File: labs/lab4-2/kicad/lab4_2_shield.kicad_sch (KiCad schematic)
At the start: 31 parts, among them J1 Digital_0-7, J2 Digital_8-13, J3 Power, J4 Analog_In, Q1 2N3904, Q2 2N3904, SW1 SW_Push, SW2 SW_Push, SW3 SW_Push, SW4 SW_Push

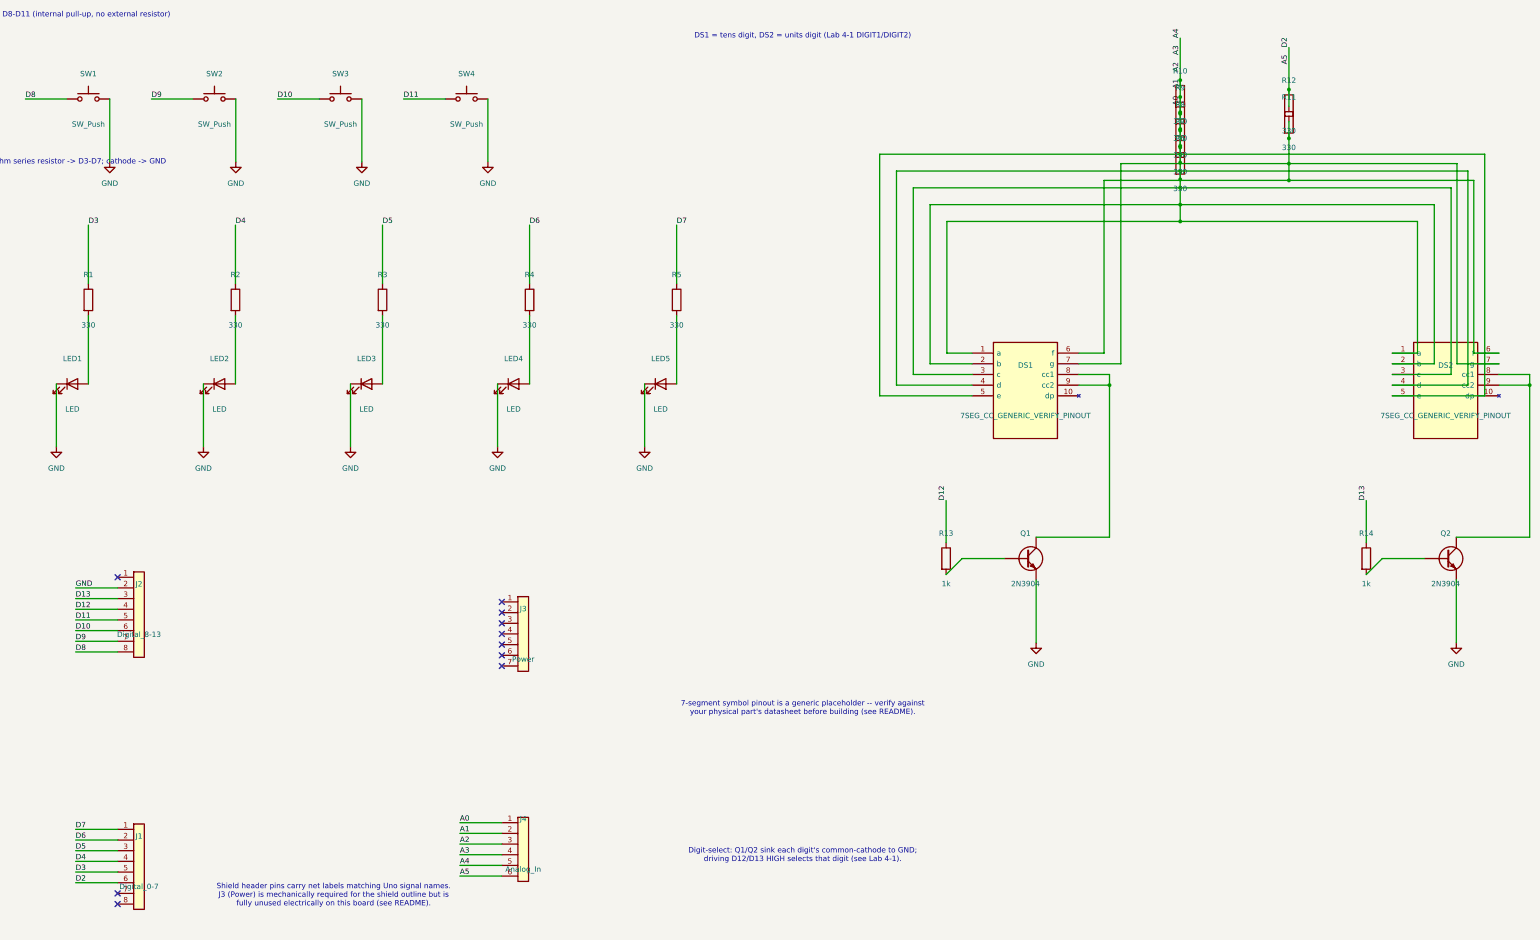
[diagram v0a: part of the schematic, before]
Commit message: feat: add LTS-6980HR 7-segment display and update KiCad project configurations
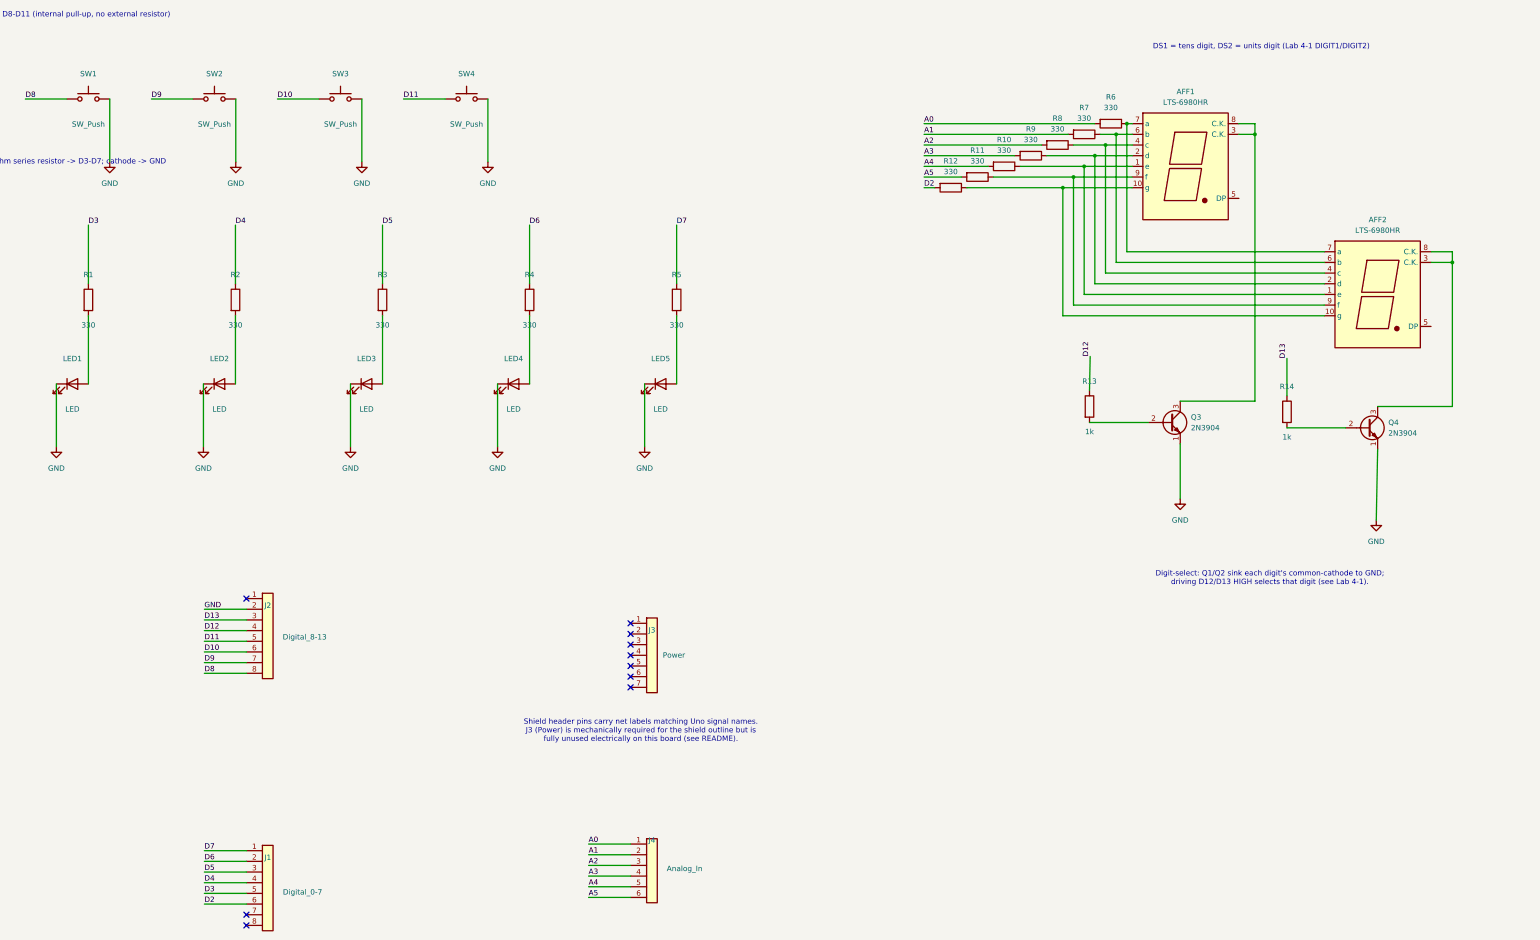
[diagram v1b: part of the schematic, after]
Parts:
- removed DS1, DS2: 7SEG_CC_GENERIC_VERIFY_PINOUT, lab4_2_shield:DISPLAY_7SEG_CC_GENERIC, symbol lab4_2_shield:DISPLAY_7SEG_CC
- removed Q1, Q2: 2N3904, Package_TO_SOT_THT:TO-92_Inline, symbol Device:Q_NPN
- added AFF1, AFF2: LTS-6980HR, Display_7Segment:7SegmentLED_LTS6760_LTS6780, symbol Display_Character:LTS-6980HR
- added Q3, Q4: 2N3904, Package_TO_SOT_THT:TO-92_Inline, symbol Transistor_BJT:2N3904
- J1, J2: footprint lab4_2_shield:Header_Shield_Female_1x08_P2.54mm -> Connector_PinHeader_2.54mm:PinHeader_1x08_P2.54mm_Vertical
- J3: footprint lab4_2_shield:Header_Shield_Female_1x07_P2.54mm -> Connector_PinHeader_2.54mm:PinHeader_1x07_P2.54mm_Vertical
- J4: footprint lab4_2_shield:Header_Shield_Female_1x06_P2.54mm -> Connector_PinHeader_2.54mm:PinHeader_1x06_P2.54mm_Vertical
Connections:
- net A0: no longer J4.2 (Pin_2), J4.3 (Pin_3), J4.4 (Pin_4), J4.5 (Pin_5), R10.1, R10.2, R6.1, R7.1, R7.2, R8.1, R8.2, R9.1, R9.2
- net A5: now also R11.2; no longer J1.6 (Pin_6), R11.1, R12.1
- net GND: now also Q3.1 (E), Q4.1 (E)
- net D2: now reaches R12.2
- net D2: now also J1.6 (Pin_6); no longer R11.2
- net at R13.2: now also Q3.2 (B)
- net at R14.2: now also Q4.2 (B)
- new net: AFF1.7 (a), AFF2.7 (a), R6.1
- new net: AFF1.6 (b), AFF2.6 (b), R7.1
- new net: AFF1.3 (C.K.), AFF1.8 (C.K.), Q3.3 (C)
- new net: AFF1.1 (e), AFF2.1 (e), R10.1
- new net: AFF1.10 (g), AFF2.10 (g), R12.1
- new net: AFF1.2 (d), AFF2.2 (d), R9.1
- new net: AFF1.4 (c), AFF2.4 (c), R8.1
- new net: AFF1.9 (f), AFF2.9 (f), R11.1
- new net: AFF2.3 (C.K.), AFF2.8 (C.K.), Q4.3 (C)
- new net A1: J4.2 (Pin_2), R7.2
- new net A2: J4.3 (Pin_3), R8.2
- new net A3: J4.4 (Pin_4), R9.2
- new net A4: J4.5 (Pin_5), R10.2
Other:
- note removed: "7-segment symbol pinout is a generic placeholder -- verify against your physical part's datasheet before building (see README)."
- moved on the sheet: J1, J2, J3, J4, R13, R14

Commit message: feat: initialize KiCad project files and PCB layout for lab 4.2 shield
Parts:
- renumbered J2 to J1, J1 to J2, Q3 to Q1, Q4 to Q2, R8 to R10, R7 to R11, R13 to R12, R6 to R13, R12 to R6, R11 to R7, R10 to R8
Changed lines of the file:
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@@
 		(in_pos_files yes)
 		(dnp no)
-		(property "Reference" "#PWR009"
+		(property "Reference" "#PWR09"
 			(at 187.49 156.95 0)
 			(hide yes)
@@
 			(project "lab4_2_shield"
 				(path "/d2732c36-58ec-418a-9ad1-28d53cb8d85c"
-					(reference "#PWR009")
+					(reference "#PWR09")
 					(unit 1)
 				)
@@
 		(dnp no)
 		(fields_autoplaced yes)
-		(property "Reference" "R6"
+		(property "Reference" "R13"
 			(at 298.45 67.31 90)
 			(show_name no)
@@
 			(project "lab4_2_shield"
 				(path "/d2732c36-58ec-418a-9ad1-28d53cb8d85c"
-					(reference "R6")
+					(reference "R13")
 					(unit 1)
 				)
@@
 		(dnp no)
 		(fields_autoplaced yes)
-		(property "Reference" "R7"
+		(property "Reference" "R11"
 			(at 292.1 69.85 90)
 			(show_name no)
@@
 			(project "lab4_2_shield"
 				(path "/d2732c36-58ec-418a-9ad1-28d53cb8d85c"
-					(reference "R7")
+					(reference "R11")
 					(unit 1)
 				)
@@
 		(dnp no)
 		(fields_autoplaced yes)
-		(property "Reference" "Q3"
+		(property "Reference" "Q1"
 			(at 317.5 143.5099 0)
 			(show_name no)
@@
 			(project "lab4_2_shield"
 				(path "/d2732c36-58ec-418a-9ad1-28d53cb8d85c"
-					(reference "Q3")
+					(reference "Q1")
 					(unit 1)
 				)
@@
 		(dnp no)
 		(fields_autoplaced yes)
-		(property "Reference" "R11"
+		(property "Reference" "R7"
 			(at 266.7 80.01 90)
 			(show_name no)
@@
 			(project "lab4_2_shield"
 				(path "/d2732c36-58ec-418a-9ad1-28d53cb8d85c"
-					(reference "R11")
+					(reference "R7")
 					(unit 1)
 				)
@@
 		(in_pos_files yes)
 		(dnp no)
-		(property "Reference" "J1"
+		(property "Reference" "J2"
 			(at 97.79 248.31 0)
 			(show_name no)
@@
 			(project "lab4_2_shield"
 				(path "/d2732c36-58ec-418a-9ad1-28d53cb8d85c"
-					(reference "J1")
+					(reference "J2")
 					(unit 1)
 				)
@@
 		(in_pos_files yes)
 		(dnp no)
-		(property "Reference" "R13"
+		(property "Reference" "R12"
 			(at 293.37 134.97 0)
 			(show_name no)
@@
 			(project "lab4_2_shield"
 				(path "/d2732c36-58ec-418a-9ad1-28d53cb8d85c"
-					(reference "R13")
+					(reference "R12")
 					(unit 1)
 				)
@@
 		(in_pos_files yes)
 		(dnp no)
-		(property "Reference" "#PWR001"
+		(property "Reference" "#PWR02"
 			(at 60.19 89.14 0)
 			(hide yes)
@@
 			(project "lab4_2_shield"
 				(path "/d2732c36-58ec-418a-9ad1-28d53cb8d85c"
-					(reference "#PWR001")
+					(reference "#PWR02")
 					(unit 1)
 				)
@@
 		(in_pos_files yes)
 		(dnp no)
-		(property "Reference" "#PWR002"
+		(property "Reference" "#PWR04"
 			(at 90.19 89.14 0)
 			(hide yes)
@@
 			(project "lab4_2_shield"
 				(path "/d2732c36-58ec-418a-9ad1-28d53cb8d85c"
-					(reference "#PWR002")
+					(reference "#PWR04")
 					(unit 1)
 				)
@@
 		(in_pos_files yes)
 		(dnp no)
-		(property "Reference" "#PWR005"
+		(property "Reference" "#PWR01"
 			(at 47.49 156.95 0)
 			(hide yes)
@@
 			(project "lab4_2_shield"
 				(path "/d2732c36-58ec-418a-9ad1-28d53cb8d85c"
-					(reference "#PWR005")
+					(reference "#PWR01")
 					(unit 1)
 				)
@@
 		(in_pos_files yes)
 		(dnp no)
-		(property "Reference" "#PWR008"
+		(property "Reference" "#PWR08"
 			(at 152.49 156.95 0)
 			(hide yes)
@@
 			(project "lab4_2_shield"
 				(path "/d2732c36-58ec-418a-9ad1-28d53cb8d85c"
-					(reference "#PWR008")
+					(reference "#PWR08")
 					(unit 1)
 				)
@@
 		(in_pos_files yes)
 		(dnp no)
-		(property "Reference" "#PWR003"
+		(property "Reference" "#PWR06"
 			(at 120.19 89.14 0)
 			(hide yes)
@@
 			(project "lab4_2_shield"
 				(path "/d2732c36-58ec-418a-9ad1-28d53cb8d85c"
-					(reference "#PWR003")
+					(reference "#PWR06")
 					(unit 1)
 				)
@@
 		(dnp no)
 		(fields_autoplaced yes)
-		(property "Reference" "R10"
+		(property "Reference" "R8"
 			(at 273.05 77.47 90)
 			(show_name no)
@@
 			(project "lab4_2_shield"
 				(path "/d2732c36-58ec-418a-9ad1-28d53cb8d85c"
-					(reference "R10")
+					(reference "R8")
 					(unit 1)
 				)
@@
 		(in_pos_files yes)
 		(dnp no)
-		(property "Reference" "#PWR006"
+		(property "Reference" "#PWR03"
 			(at 82.49 156.95 0)
 			(hide yes)
@@
 			(project "lab4_2_shield"
 				(path "/d2732c36-58ec-418a-9ad1-28d53cb8d85c"
-					(reference "#PWR006")
+					(reference "#PWR03")
 					(unit 1)
 				)
@@
 		(in_pos_files yes)
 		(dnp no)
-		(property "Reference" "#PWR007"
+		(property "Reference" "#PWR05"
 			(at 117.49 156.95 0)
 			(hide yes)
@@
 			(project "lab4_2_shield"
 				(path "/d2732c36-58ec-418a-9ad1-28d53cb8d85c"
-					(reference "#PWR007")
+					(reference "#PWR05")
 					(unit 1)
 				)
@@
 		(dnp no)
 		(fields_autoplaced yes)
-		(property "Reference" "R12"
+		(property "Reference" "R6"
 			(at 260.35 82.55 90)
 			(show_name no)
@@
 			(project "lab4_2_shield"
 				(path "/d2732c36-58ec-418a-9ad1-28d53cb8d85c"
-					(reference "R12")
+					(reference "R6")
 					(unit 1)
 				)
@@
 		(dnp no)
 		(fields_autoplaced yes)
-		(property "Reference" "R8"
+		(property "Reference" "R10"
 			(at 285.75 72.39 90)
 			(show_name no)
@@
 			(project "lab4_2_shield"
 				(path "/d2732c36-58ec-418a-9ad1-28d53cb8d85c"
-					(reference "R8")
+					(reference "R10")
 					(unit 1)
 				)
@@
 		(in_pos_files yes)
 		(dnp no)
-		(property "Reference" "#PWR004"
+		(property "Reference" "#PWR07"
 			(at 150.19 89.14 0)
 			(hide yes)
@@
 			(project "lab4_2_shield"
 				(path "/d2732c36-58ec-418a-9ad1-28d53cb8d85c"
-					(reference "#PWR004")
+					(reference "#PWR07")
 					(unit 1)
 				)
@@
 		(dnp no)
 		(fields_autoplaced yes)
-		(property "Reference" "Q4"
+		(property "Reference" "Q2"
 			(at 364.49 144.7799 0)
 			(show_name no)
@@
 			(project "lab4_2_shield"
 				(path "/d2732c36-58ec-418a-9ad1-28d53cb8d85c"
-					(reference "Q4")
+					(reference "Q2")
 					(unit 1)
 				)
@@
 		(in_pos_files yes)
 		(dnp no)
-		(property "Reference" "J2"
+		(property "Reference" "J1"
 			(at 97.79 188.31 0)
 			(show_name no)
@@
 			(project "lab4_2_shield"
 				(path "/d2732c36-58ec-418a-9ad1-28d53cb8d85c"
-					(reference "J2")
-					(unit 1)
-				)
+					(reference "J1")
+					(unit 1)
+				)

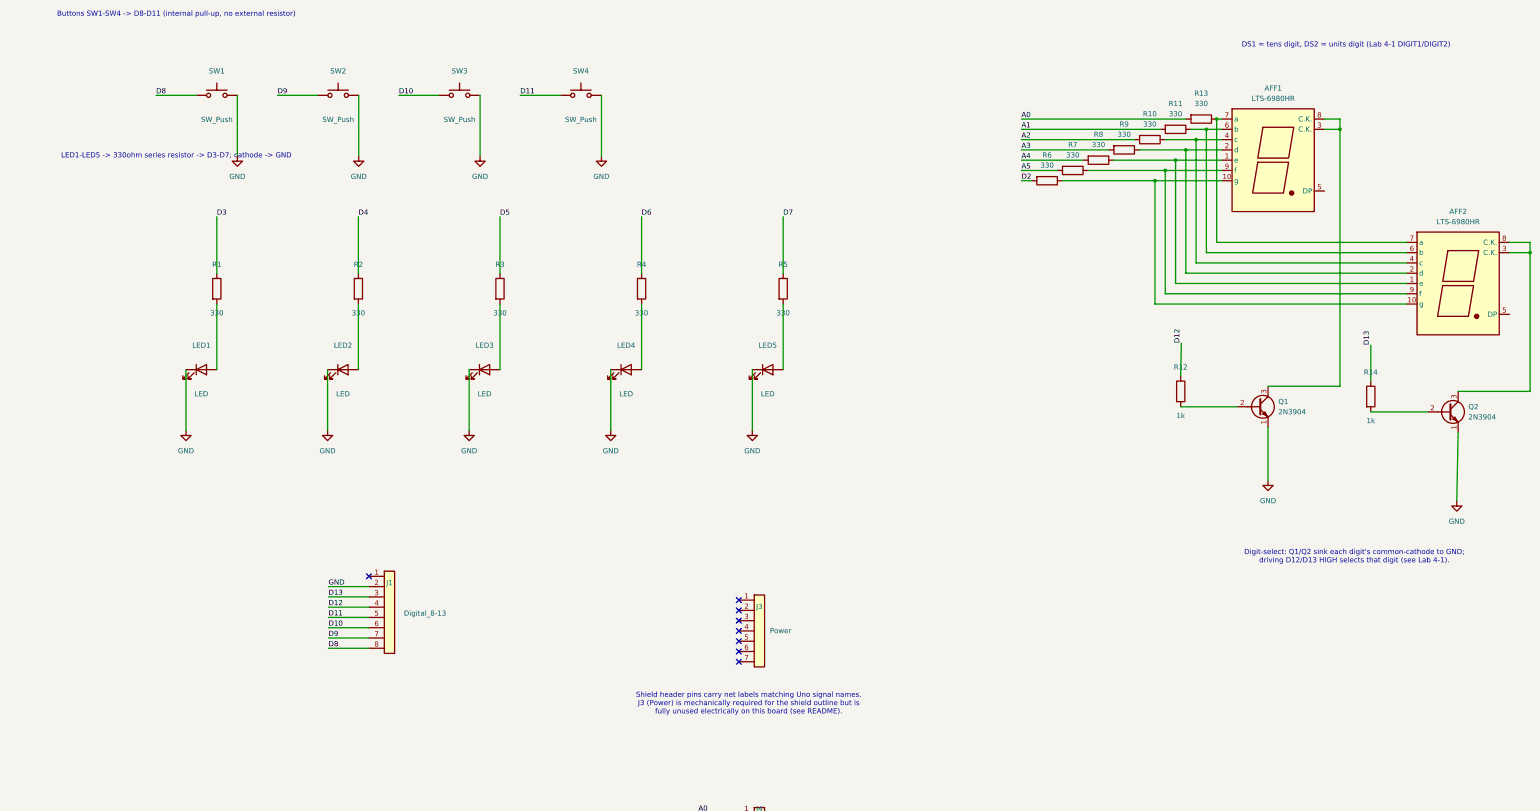
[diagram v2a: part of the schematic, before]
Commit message: refactor: update text label coordinates and component placements in KiCad project files
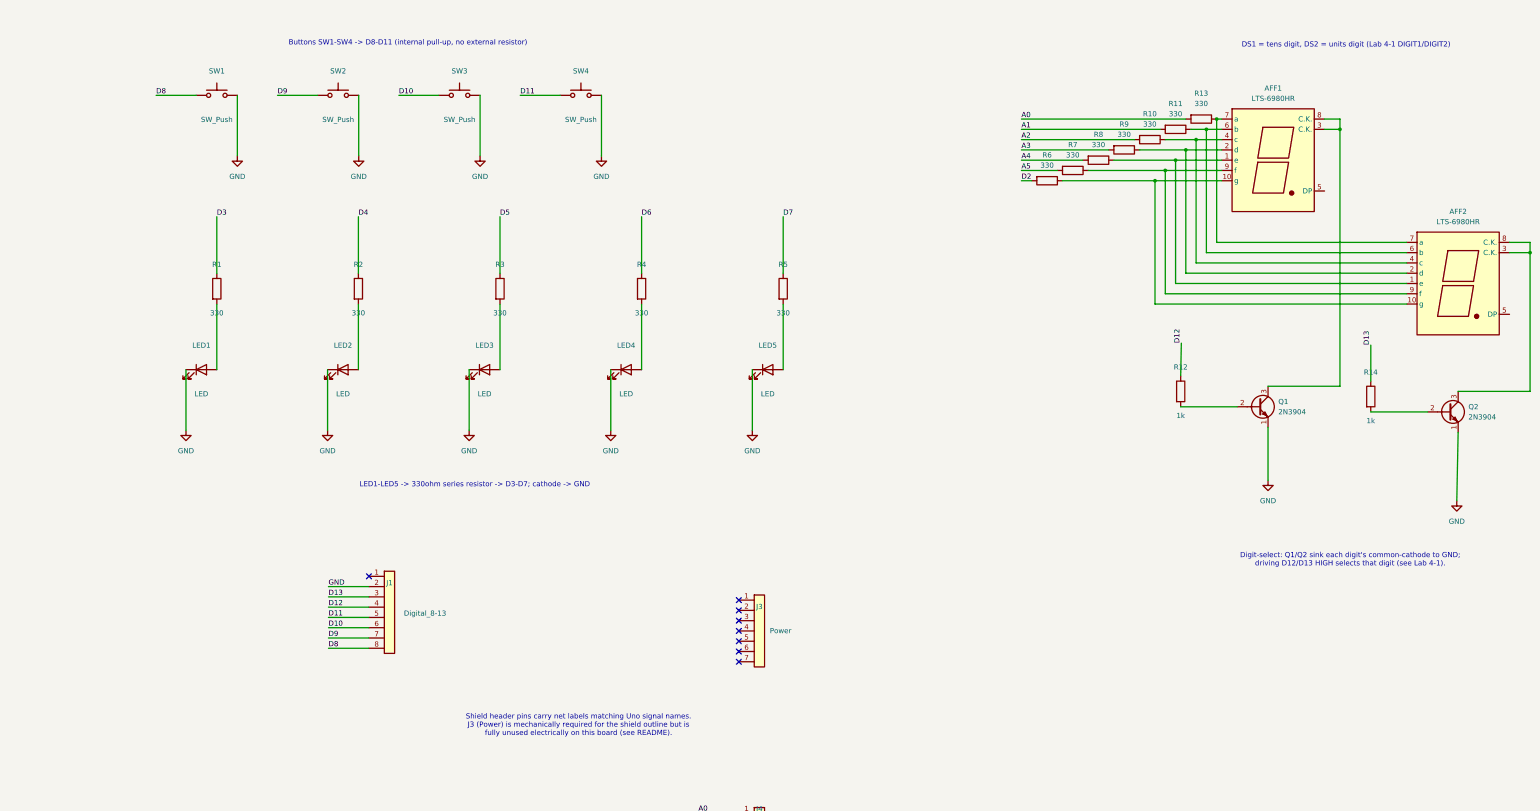
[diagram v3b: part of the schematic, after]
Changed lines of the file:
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@@
 	(text "Digit-select: Q1/Q2 sink each digit's common-cathode to GND;\ndriving D12/D13 HIGH selects that digit (see Lab 4-1)."
 		(exclude_from_sim no)
-		(at 336.296 181.864 0)
+		(at 335.28 182.626 0)
 		(effects
 			(font
@@
 	(text "Buttons SW1-SW4 -> D8-D11 (internal pull-up, no external resistor)"
 		(exclude_from_sim no)
-		(at 45.11 47.79 0)
+		(at 102.362 54.864 0)
 		(effects
 			(font
@@
 	(text "Shield header pins carry net labels matching Uno signal names.\nJ3 (Power) is mechanically required for the shield outline but is\nfully unused electrically on this board (see README)."
 		(exclude_from_sim no)
-		(at 186.596 218.186 0)
+		(at 144.526 223.52 0)
 		(effects
 			(font
@@
 	(text "LED1-LED5 -> 330ohm series resistor -> D3-D7; cathode -> GND"
 		(exclude_from_sim no)
-		(at 45.11 82.79 0)
+		(at 118.872 164.084 0)
 		(effects
 			(font
